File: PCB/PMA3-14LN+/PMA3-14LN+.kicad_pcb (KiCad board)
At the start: 4 copper layers, 55.3 x 35 mm, 25 parts, among them IC1 PMA3-14LN+, U1 L7806

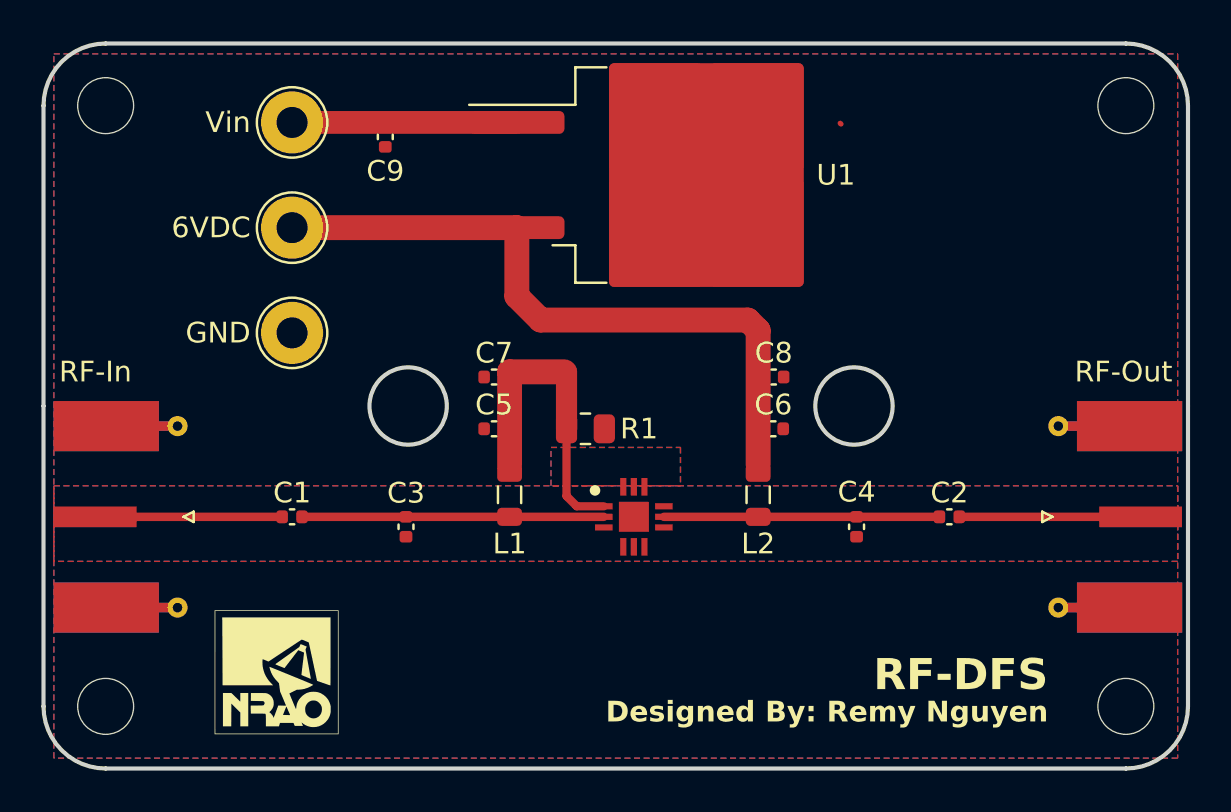
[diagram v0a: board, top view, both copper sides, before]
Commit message: PMA3-14LN+ design complete sans signal launch tuning
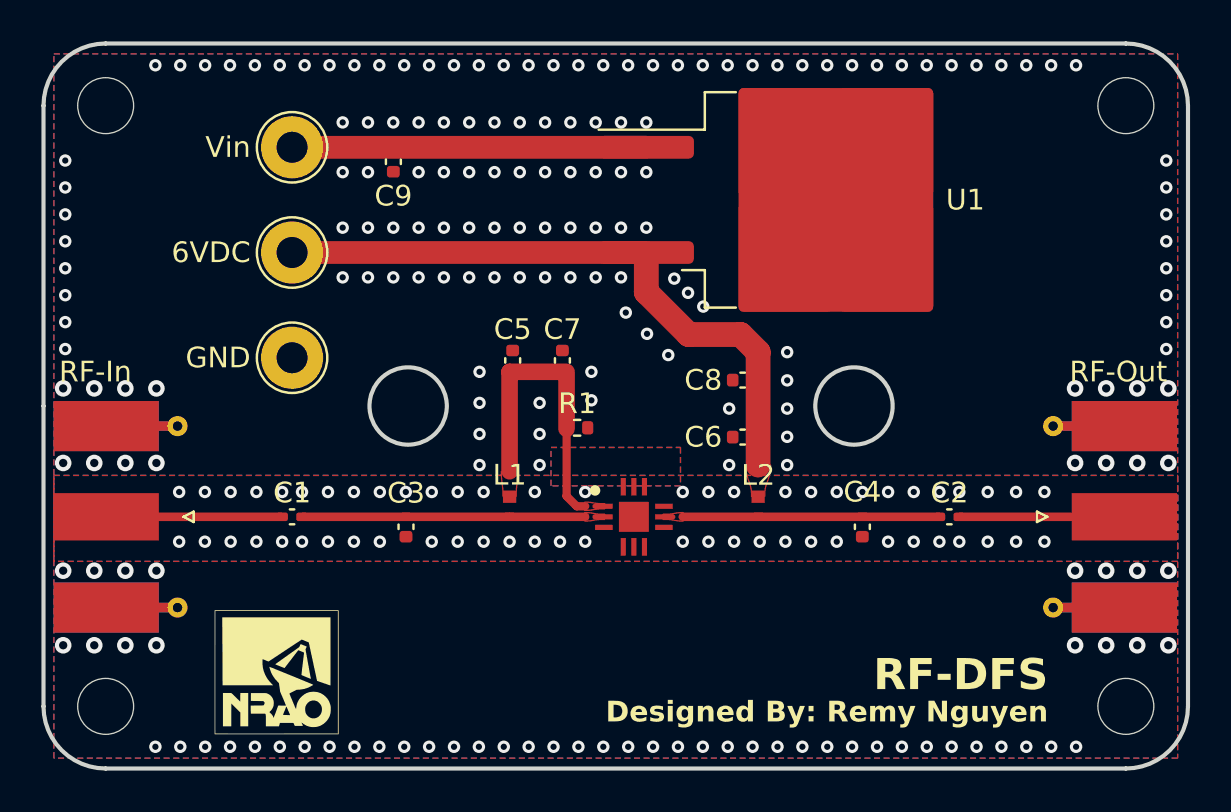
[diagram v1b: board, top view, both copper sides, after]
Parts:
- added ?: , imports:RF-DFS-GCPW-OSH, F.Cu at (207.0, 147.5)
- L1, L2: footprint Inductor_SMD:L_0805_2012Metric -> Inductor_SMD:L_0402_1005Metric
- R1: footprint Resistor_SMD:R_0805_2012Metric -> Resistor_SMD:R_0402_1005Metric
- moved U1 6.36 mm to (147.6, 78.7)
- moved C5 3.42 mm to (133.5, 86.5), turned to -90 degrees
- moved C7 3.40 mm to (135.9, 86.5), turned to -90 degrees
- moved C6 1.53 mm to (144.6, 90.2), turned to 180 degrees
- moved C8 1.51 mm to (144.6, 87.4), turned to 180 degrees
- moved C9 1.26 mm to (127.7, 76.9)
- moved Vin 1.20 mm to (122.8, 76.2)
- moved 6VDC 1.20 mm to (122.8, 81.2)
- moved GND 1.20 mm to (122.8, 86.3)
- moved L1 0.58 mm to (133.3, 93.5)
- moved L2 0.58 mm to (145.3, 93.5)
- moved R1 0.41 mm to (136.6, 89.7)
- moved C4 0.28 mm to (150.4, 94.5)
- moved RF-Out 0.25 mm to (161.3, 94.0)
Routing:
- net Vin: track 10.8 -> 17.1 mm
- net 6VDC: track 33.0 -> 30.5 mm
- net GND: track 0.17 -> 0.06 mm, vias 0 -> 255
- added copper zone on F.Cu, net 6VDC
- added copper zone on F.Cu, net Net-(IC1-CURRENT_MIRROR)
- added copper zone on F.Cu, net Net-(IC1-RF-IN)
- added copper zone on F.Cu, net Net-(IC1-RF-OUT_&_VDD)
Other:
- rule solder_mask_min_width: 0.25 -> 0.1016
- board text added: "4/12/2024"
- board text added: "50-10000 MHz SMT LNA"
- board text added: "A"
- board text added: "BOT-L4"
- board text added: "IN-L2"
- board text added: "IN-L3"
- board text added: "Remy Nguyen"
- board text added: "TOP-L1"

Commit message: Updated silkscreen and reference designators on EMS boards
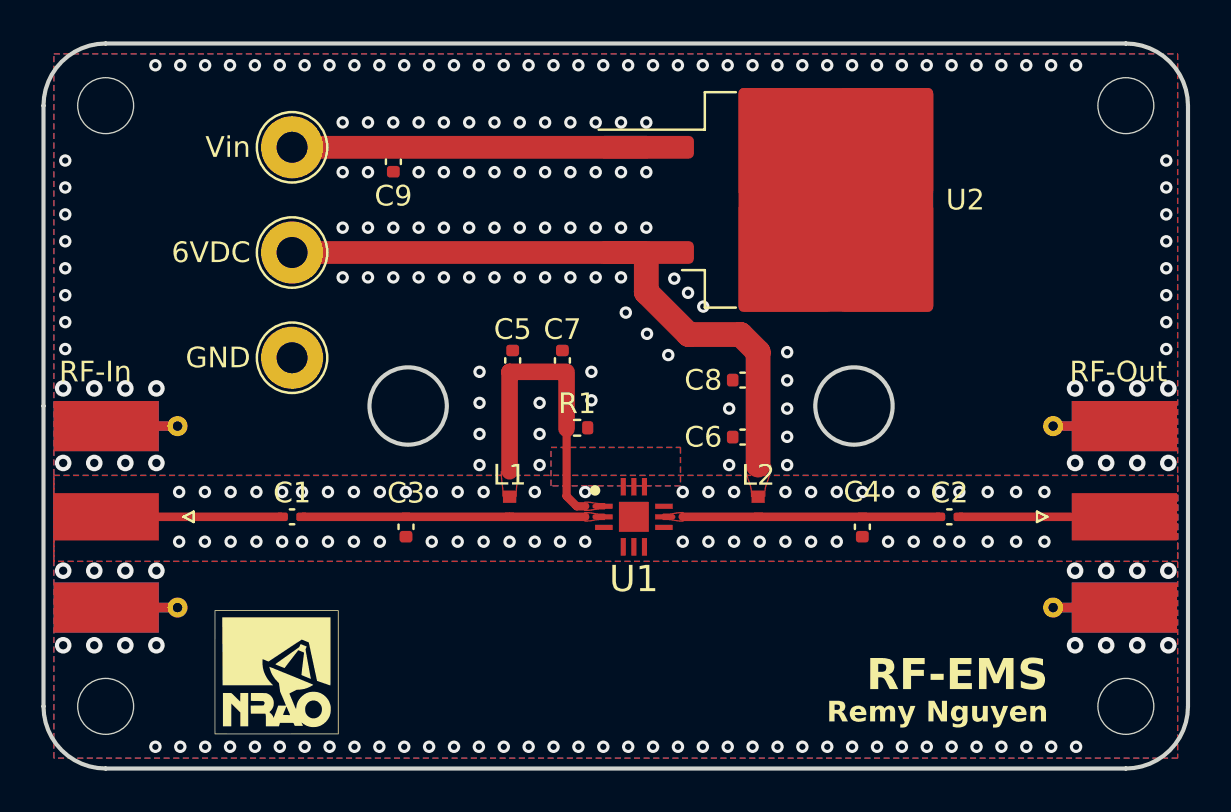
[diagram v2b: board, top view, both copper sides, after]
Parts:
- renumbered IC1 to U1, U1 to U2
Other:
- board text added: "PMA3-14LN+"
- board text added: "RF-EMS"
- board text removed: "Designed By: Remy Nguyen"
- board text removed: "RF-DFS"
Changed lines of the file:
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@@
     (property "ki_keywords" "Voltage Regulator 1.5A Positive")
     (attr smd)
-    (fp_text reference "U1" (at 7.75 0) (layer "F.SilkS")
+    (fp_text reference "U2" (at 7.75 0) (layer "F.SilkS")
         (effects (font (size 1 1) (thickness 0.15)))
     )
@@
     (solder_mask_margin 0.04)
     (attr smd)
-    (fp_text reference "IC1" (at 0 0) (layer "F.SilkS") hide
+    (fp_text reference "U1" (at 0 3) (layer "F.SilkS")
         (effects (font (size 1.27 1.27) (thickness 0.254)))
     )
@@
   (gr_line (start 128.45 88.56) (end 128.45 88.74)
     (stroke (width 0.2) (type solid)) (layer "User.9"))
-  (gr_text "RF-DFS" (at 159.35 102.5) (layer "F.SilkS")
+  (gr_text "PMA3-14LN+" (at 159.35 104) (layer "B.SilkS")
+    (effects (font (size 1 1) (thickness 0.2) bold) (justify left bottom mirror))
+  )
+  (gr_text "RF-EMS" (at 159.35 102.5) (layer "F.SilkS")
     (effects (font (size 1.5 1.5) (thickness 0.3) bold) (justify right bottom))
   )
-  (gr_text "Designed By: Remy Nguyen" (at 159.35 104) (layer "F.SilkS")
+  (gr_text "Remy Nguyen" (at 159.35 104) (layer "F.SilkS")
     (effects (font (size 1 1) (thickness 0.2) bold) (justify right bottom))
   )

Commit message: PMA-183PLN+ PCB Rev A completed
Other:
- board text added: "Hole pattern for Hammond 1554B"
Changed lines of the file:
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@@
     (fp_line (start 5.625 5) (end 4.625 5)
       (stroke (width 0.1) (type solid)) (layer "F.Fab"))
-    (pad "1" smd roundrect (at -7.65 -2.54) (size 4.6 1.1) (layers "F.Cu" "F.Paste" "F.Mask") (roundrect_rratio 0.227273)
+    (pad "1" smd roundrect (at -7.65 -2.54) (size 4.6 1.1) (layers "F.Cu" "F.Paste" "F.Mask") (roundrect_rratio 0.2272727273)
       (net 8 "Vin") (pinfunction "IN") (pintype "power_in"))
-    (pad "2" smd roundrect (at -0.925 -2.775) (size 4.55 5.25) (layers "F.Cu" "F.Paste") (roundrect_rratio 0.054945)
+    (pad "2" smd roundrect (at -0.925 -2.775) (size 4.55 5.25) (layers "F.Cu" "F.Paste") (roundrect_rratio 0.05494505495)
       (net 5 "GND") (pinfunction "GND") (pintype "power_in"))
-    (pad "2" smd roundrect (at -0.925 2.775) (size 4.55 5.25) (layers "F.Cu" "F.Paste") (roundrect_rratio 0.054945)
+    (pad "2" smd roundrect (at -0.925 2.775) (size 4.55 5.25) (layers "F.Cu" "F.Paste") (roundrect_rratio 0.05494505495)
       (net 5 "GND") (pinfunction "GND") (pintype "power_in"))
-    (pad "2" smd roundrect (at 1.5 0) (size 9.4 10.8) (layers "F.Cu" "F.Mask") (roundrect_rratio 0.026596)
+    (pad "2" smd roundrect (at 1.5 0) (size 9.4 10.8) (layers "F.Cu" "F.Mask") (roundrect_rratio 0.02659595745)
       (net 5 "GND") (pinfunction "GND") (pintype "power_in"))
-    (pad "2" smd roundrect (at 3.925 -2.775) (size 4.55 5.25) (layers "F.Cu" "F.Paste") (roundrect_rratio 0.054945)
+    (pad "2" smd roundrect (at 3.925 -2.775) (size 4.55 5.25) (layers "F.Cu" "F.Paste") (roundrect_rratio 0.05494505495)
       (net 5 "GND") (pinfunction "GND") (pintype "power_in"))
-    (pad "2" smd roundrect (at 3.925 2.775) (size 4.55 5.25) (layers "F.Cu" "F.Paste") (roundrect_rratio 0.054945)
+    (pad "2" smd roundrect (at 3.925 2.775) (size 4.55 5.25) (layers "F.Cu" "F.Paste") (roundrect_rratio 0.05494505495)
       (net 5 "GND") (pinfunction "GND") (pintype "power_in"))
-    (pad "3" smd roundrect (at -7.65 2.54) (size 4.6 1.1) (layers "F.Cu" "F.Paste" "F.Mask") (roundrect_rratio 0.227273)
+    (pad "3" smd roundrect (at -7.65 2.54) (size 4.6 1.1) (layers "F.Cu" "F.Paste" "F.Mask") (roundrect_rratio 0.2272727273)
       (net 7 "6VDC") (pinfunction "OUT") (pintype "power_out"))
     (model "${KICAD6_3DMODEL_DIR}/Package_TO_SOT_SMD.3dshapes/TO-263-2.wrl"
@@
     (effects (font (size 1 1) (thickness 0.2) bold) (justify right bottom))
   )
+  (gr_text "Hole pattern for Hammond 1554B" (at 159.85 173.45) (layer "Cmts.User")
+    (effects (font (size 1.5 1.5) (thickness 0.3) bold) (justify left))
+  )
   (gr_text "Remy Nguyen" (at 266.5 185.5) (layer "Cmts.User")
